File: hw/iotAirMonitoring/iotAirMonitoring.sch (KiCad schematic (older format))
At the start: 69 parts, among them J1 MQ-7, J2 VEML7700, J3 SHT40, J4 PROGRAMMER, J5 ML8511, J6 EN_3V3_PROGRAMMER, J7 BMP388, J8 PMS5003, Q1 MMBT3904, Q2 MMBT3904, Q3 AO3401A, Q4 2N7002, Q5 AO3401A, Q6 2N7002, Q7 AO3401A, Q8 2N7002, SW1 SW_Push, SW2 SW_Push, SW3 RESET, SW4 SW_Push, U1 ESP32-WROOM-32, U2 MCP3202-BI/SN

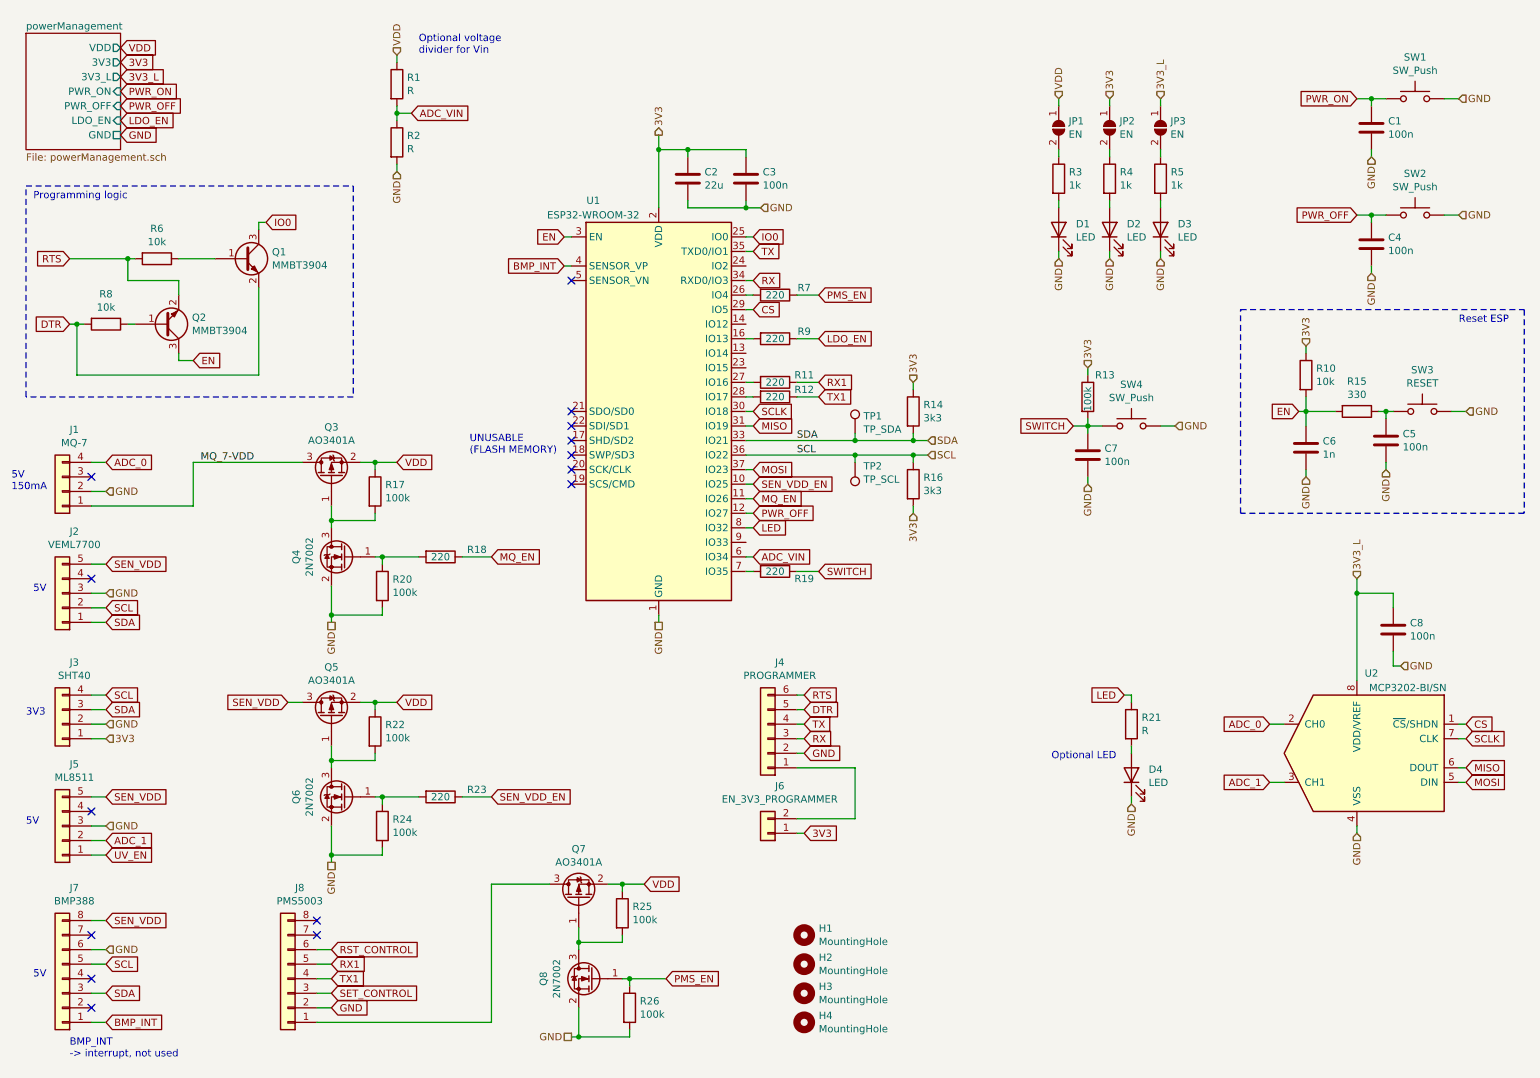
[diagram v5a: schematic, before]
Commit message: Nearly finished schematic, add optional LoRa module
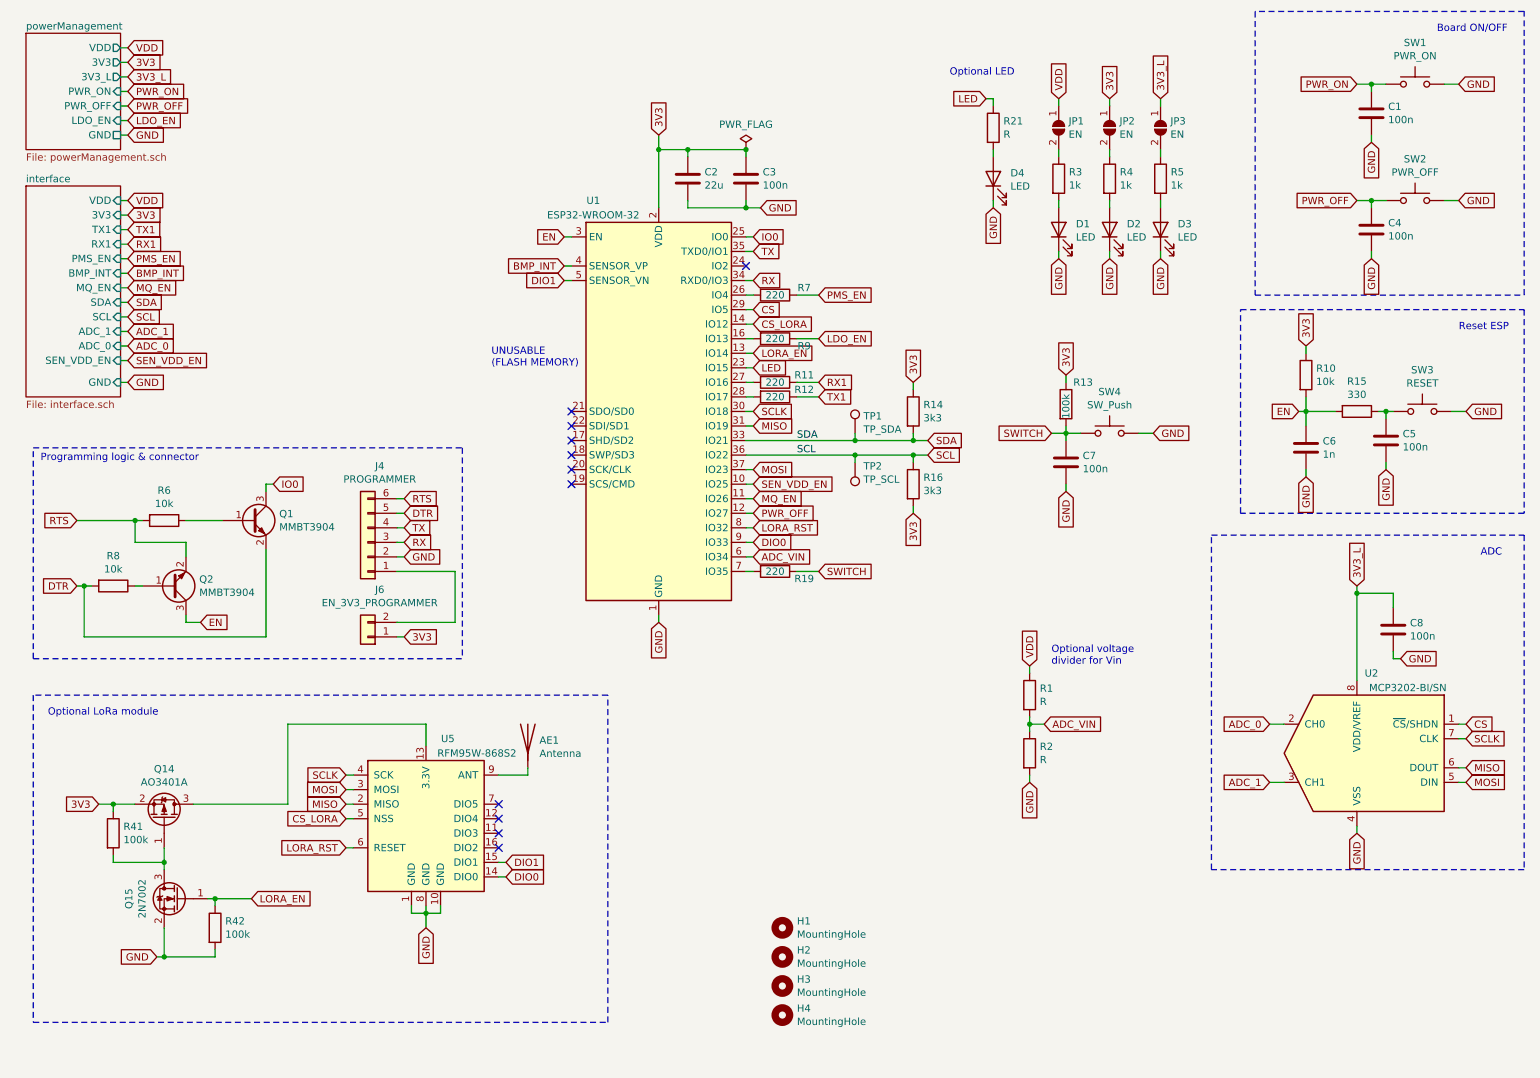
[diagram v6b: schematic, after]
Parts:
- removed J1: MQ-7, Connector_PinSocket_2.54mm:PinSocket_1x04_P2.54mm_Vertical, symbol Connector_Generic:Conn_01x04
- removed J2: VEML7700, Connector_PinSocket_2.54mm:PinSocket_1x05_P2.54mm_Vertical, symbol Connector_Generic:Conn_01x05
- removed J3: SHT40, Connector_PinSocket_2.54mm:PinSocket_1x04_P2.54mm_Vertical, symbol Connector_Generic:Conn_01x04
- removed J5: ML8511, Connector_PinSocket_2.54mm:PinSocket_1x05_P2.54mm_Vertical, symbol Connector_Generic:Conn_01x05
- removed J7: BMP388, Connector_PinSocket_2.54mm:PinSocket_1x08_P2.54mm_Vertical, symbol Connector_Generic:Conn_01x08
- removed J8: PMS5003, symbol Connector_Generic:Conn_01x08
- removed Q3, Q5, Q7: AO3401A, Package_TO_SOT_SMD:SOT-23, symbol Device:Q_PMOS_GSD
- removed Q4, Q6, Q8: 2N7002, Package_TO_SOT_SMD:SOT-23, symbol Transistor_FET:2N7002
- removed R17, R20, R22, R24, R25, R26: 100k, Resistor_SMD:R_0402_1005Metric, symbol Device:R
- removed R18, R23: 220, Resistor_SMD:R_0402_1005Metric, symbol Device:R
- added AE1: Antenna, RF_Antenna:Texas_SWRA416_868MHz_915MHz, symbol Device:Antenna
- added Q14: AO3401A, Package_TO_SOT_SMD:SOT-23, symbol Device:Q_PMOS_GSD
- added Q15: 2N7002, Package_TO_SOT_SMD:SOT-23, symbol Transistor_FET:2N7002
- added R41, R42: 100k, Resistor_SMD:R_0402_1005Metric, symbol Device:R
- added U5: RFM95W-868S2, RF_Module:HOPERF_RFM9XW_THT, symbol RF_Module:RFM95W-868S2
- SW1: value SW_Push -> PWR_ON
- SW2: value SW_Push -> PWR_OFF
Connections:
- net 3V3: now also Q14.2 (S), R41.1
- net GND: now also Q15.2 (S), R42.2, U5.1 (GND), U5.10 (GND), U5.8 (GND)
- net LED: now also U1.23 (IO15); no longer U1.8 (IO32)
- net MISO: now also U5.2 (MISO)
- net MOSI: now also U5.3 (MOSI)
- net SCLK: now also U5.4 (SCK)
- net LORA_EN: now reaches U1.13 (IO14)
- net LORA_EN: now also Q15.1 (G), R42.1
- net CS_LORA: now reaches U1.14 (IO12)
- net CS_LORA: now also U5.5 (NSS)
- net DIO1: now reaches U1.5 (SENSOR_VN)
- net DIO1: now also U5.15 (DIO1)
- net DIO0: now reaches U1.9 (IO33)
- net DIO0: now also U5.14 (DIO0)
- new net: Q14.3 (D), U5.13 (3.3V)
- new net: AE1.1 (A), U5.9 (ANT)
- new net: Q14.1 (G), Q15.3 (D), R41.2
- new net LORA_RST: U1.8 (IO32), U5.6 (RESET)
- no-connect marks 15 -> 11
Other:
- note added: "ADC"
- note added: "Board ON/OFF"
- note added: "Optional LoRa module"
- note added: "Programming logic & connector"
- note removed: "3V3"
- note removed: "5V"
- note removed: "5V\n150mA"
- note removed: "BMP_INT\n-> interrupt, not used"
- note removed: "Programming logic"
- moved on the sheet: C1, C4, C7, D4, H1, H2, H3, H4, J4, J6, Q1, Q2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

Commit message: More routing on main board
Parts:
- added TP3: TP_RX1, TestPoint:TestPoint_Pad_D1.5mm, symbol Connector:TestPoint
- added TP4: TP_TX1, TestPoint:TestPoint_Pad_D1.5mm, symbol Connector:TestPoint
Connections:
- net RX1: now also TP3.1
- net TX1: now also TP4.1
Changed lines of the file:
@@
 encoding utf-8
 Sheet 1 3
-Title ""
+Title "iotAirMonitoring"
 Date ""
-Rev ""
+Rev "v0.1"
 Comp ""
 Comment1 ""
@@
 Text GLabel 1450 3100 2    50   Input ~ 0
 GND
+$Comp
+L Connector:TestPoint TP3
+U 1 1 6181341E
+P 6450 5150
+F 0 "TP3" V 6350 5150 50  0000 L CNN
+F 1 "TP_RX1" V 6450 5350 50  0000 L CNN
+F 2 "TestPoint:TestPoint_Pad_D1.5mm" H 6650 5150 50  0001 C CNN
+F 3 "~" H 6650 5150 50  0001 C CNN
+	1    6450 5150
+	0    1    1    0
+$EndComp
+$Comp
+L Connector:TestPoint TP4
+U 1 1 618164A5
+P 6450 5350
+F 0 "TP4" V 6350 5350 50  0000 L CNN
+F 1 "TP_TX1" V 6450 5550 50  0000 L CNN
+F 2 "TestPoint:TestPoint_Pad_D1.5mm" H 6650 5350 50  0001 C CNN
+F 3 "~" H 6650 5350 50  0001 C CNN
+	1    6450 5350
+	0    1    1    0
+$EndComp
+Wire Wire Line
+	6450 5150 6400 5150
+Wire Wire Line
+	6450 5350 6400 5350
+Text GLabel 6400 5150 0    50   Input ~ 0
+RX1
+Text GLabel 6400 5350 0    50   Input ~ 0
+TX1
 $EndSCHEMATC
